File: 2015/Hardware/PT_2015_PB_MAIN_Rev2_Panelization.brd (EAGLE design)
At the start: 142.5 x 234.8 mm, 161 parts, among them Q1 Q_ACS711LC_SKETCH, Q11 Q_IRFS7437PbF, Q12 2N7002, Q14 Q_IRFS7437PbF, Q16 Q_IRFS7437PbF, Q18 Q_FDT86102LZ, Q20 Q_IRFS7437PbF, Q4 Q_ACS711LC, Q5 Q_ACS711LC, Q6 Q_IRFS7437PbF, Q7 Q_IRFS7437PbF, Q9 Q_IRFS7437PbF

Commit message: Cleaned up my idiotic TSTOP
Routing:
- net N$33: track 10.2 -> 0.00 mm
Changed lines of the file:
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@@
 <vertex x="5.08" y="2.54"/>
 </polygon>
-<dimension x1="137.795" y1="166.37" x2="137.795" y2="-67.945" x3="180.34" y3="49.2125" textsize="1.778" layer="21" unit="inch"/>
 <wire x1="1.27" y1="-8.89" x2="104.14" y2="-8.89" width="0.4064" layer="21"/>
 <wire x1="1.27" y1="-8.89" x2="1.27" y2="-52.07" width="0.4064" layer="21"/>
@@
 <wire x1="73.66" y1="-52.07" x2="104.14" y2="-52.07" width="0.4064" layer="21"/>
 <wire x1="104.14" y1="-52.07" x2="104.14" y2="-8.89" width="0.4064" layer="21"/>
+<dimension x1="137.795" y1="166.37" x2="137.541" y2="-68.453" x3="165.69279375" y3="48.928184375" textsize="3.81" layer="29" unit="inch" visible="yes"/>
 <polygon width="0.8128" layer="29">
-<vertex x="45.466" y="119.888"/>
-<vertex x="45.466" y="110.998"/>
-<vertex x="40.894" y="110.998"/>
-<vertex x="40.894" y="103.886"/>
-<vertex x="45.466" y="103.886"/>
-<vertex x="57.658" y="103.886"/>
-<vertex x="57.658" y="105.918"/>
-<vertex x="51.562" y="105.918"/>
-<vertex x="51.562" y="109.728"/>
-<vertex x="51.562" y="111.506"/>
-<vertex x="62.992" y="111.506"/>
-<vertex x="75.184" y="111.506"/>
-<vertex x="75.184" y="105.918"/>
-<vertex x="69.342" y="105.918"/>
-<vertex x="69.342" y="104.14"/>
-<vertex x="82.042" y="104.14"/>
-<vertex x="82.042" y="120.396"/>
-<vertex x="45.466" y="120.396"/>
+<vertex x="71.882" y="1.27"/>
+<vertex x="71.882" y="1.27"/>
+<vertex x="72.136" y="1.27"/>
 </polygon>
 <polygon width="0.8128" layer="29">
-<vertex x="57.658" y="104.902"/>
-<vertex x="69.342" y="104.902"/>
-<vertex x="69.342" y="104.14"/>
-<vertex x="57.658" y="104.14"/>
-<vertex x="57.658" y="103.886"/>
-</polygon>
-<polygon width="0.8128" layer="29">
-<vertex x="63.754" y="104.394"/>
-<vertex x="63.754" y="101.854"/>
-<vertex x="64.516" y="101.854" curve="-90"/>
-<vertex x="71.12" y="95.25" curve="-96.025575"/>
-<vertex x="63.5" y="88.392"/>
-<vertex x="63.5" y="83.058"/>
-<vertex x="64.516" y="83.058" curve="-90"/>
-<vertex x="71.374" y="76.2" curve="-97.62815"/>
-<vertex x="63.246" y="69.088"/>
-<vertex x="63.5" y="69.088"/>
-<vertex x="63.5" y="64.008"/>
-<vertex x="64.516" y="64.008" curve="-90"/>
-<vertex x="71.374" y="57.15" curve="-95.631113"/>
-<vertex x="63.246" y="49.784"/>
-<vertex x="63.246" y="44.958"/>
-<vertex x="64.77" y="44.958" curve="-90"/>
-<vertex x="71.628" y="38.1" curve="-90"/>
-<vertex x="64.516" y="30.988"/>
-<vertex x="63.246" y="30.988"/>
-<vertex x="63.246" y="6.35"/>
-<vertex x="81.026" y="6.35"/>
-<vertex x="81.026" y="23.622"/>
-<vertex x="79.248" y="23.622"/>
-<vertex x="79.248" y="26.67"/>
-<vertex x="81.026" y="26.67"/>
-<vertex x="81.026" y="53.594"/>
-<vertex x="80.01" y="53.594"/>
-<vertex x="80.01" y="104.14"/>
-<vertex x="73.914" y="104.14"/>
-<vertex x="73.914" y="104.394"/>
-</polygon>
-<polygon width="0.8128" layer="29">
-<vertex x="62.992" y="104.648"/>
-<vertex x="62.992" y="102.108"/>
-<vertex x="62.738" y="102.108" curve="90"/>
-<vertex x="56.642" y="96.012"/>
-<vertex x="56.642" y="94.742"/>
-<vertex x="56.642" y="94.488" curve="90"/>
-<vertex x="62.738" y="88.392" curve="-90"/>
-<vertex x="62.992" y="88.138"/>
-<vertex x="62.992" y="83.058"/>
-<vertex x="62.738" y="83.058" curve="90"/>
-<vertex x="56.642" y="76.962"/>
-<vertex x="56.642" y="75.692" curve="90"/>
-<vertex x="63.246" y="69.088"/>
-<vertex x="63.246" y="64.008"/>
-<vertex x="62.992" y="64.008" curve="90"/>
-<vertex x="56.642" y="57.658"/>
-<vertex x="56.642" y="56.642" curve="90"/>
-<vertex x="62.738" y="50.546"/>
-<vertex x="62.738" y="45.212" curve="90"/>
-<vertex x="56.642" y="39.116"/>
-<vertex x="56.642" y="37.592" curve="90"/>
-<vertex x="62.992" y="31.242"/>
-<vertex x="63.246" y="31.242"/>
-<vertex x="63.246" y="-1.778"/>
-<vertex x="60.198" y="-1.778"/>
-<vertex x="51.562" y="-1.778"/>
-<vertex x="49.784" y="0"/>
-<vertex x="48.514" y="1.27"/>
-<vertex x="48.514" y="2.54"/>
-<vertex x="48.514" y="3.302"/>
-<vertex x="47.498" y="3.302"/>
-<vertex x="47.498" y="5.334"/>
+<vertex x="45.974" y="120.65"/>
+<vertex x="45.974" y="110.236"/>
+<vertex x="41.402" y="110.236"/>
+<vertex x="41.402" y="104.394"/>
+<vertex x="45.974" y="104.394"/>
+<vertex x="45.974" y="93.726"/>
+<vertex x="41.402" y="93.726"/>
+<vertex x="41.402" y="87.884"/>
+<vertex x="45.974" y="87.884"/>
+<vertex x="45.974" y="77.216"/>
+<vertex x="41.402" y="77.216"/>
+<vertex x="41.402" y="71.374"/>
+<vertex x="45.974" y="71.374"/>
+<vertex x="45.974" y="60.706"/>
+<vertex x="41.402" y="60.706"/>
+<vertex x="41.402" y="54.864"/>
+<vertex x="45.974" y="54.864"/>
+<vertex x="45.974" y="44.196"/>
+<vertex x="41.402" y="44.196"/>
+<vertex x="41.402" y="38.354"/>
+<vertex x="45.974" y="38.354"/>
+<vertex x="45.974" y="27.686"/>
+<vertex x="41.402" y="27.686"/>
+<vertex x="41.402" y="21.844"/>
+<vertex x="45.974" y="21.844"/>
+<vertex x="45.974" y="11.176"/>
+<vertex x="41.402" y="11.176"/>
 <vertex x="41.402" y="5.334"/>
-<vertex x="41.402" y="11.176"/>
-<vertex x="45.72" y="11.176"/>
-<vertex x="45.974" y="11.176"/>
-<vertex x="45.974" y="21.844"/>
-<vertex x="41.402" y="21.844"/>
-<vertex x="41.402" y="27.686"/>
-<vertex x="45.974" y="27.686"/>
-<vertex x="45.974" y="38.354"/>
-<vertex x="45.72" y="38.354"/>
-<vertex x="41.402" y="38.354"/>
-<vertex x="41.402" y="44.196"/>
-<vertex x="45.974" y="44.196"/>
-<vertex x="45.974" y="54.864"/>
-<vertex x="41.402" y="54.864"/>
-<vertex x="41.402" y="60.706"/>
-<vertex x="46.228" y="60.706"/>
-<vertex x="45.974" y="60.706"/>
-<vertex x="45.974" y="71.374"/>
-<vertex x="41.402" y="71.374"/>
-<vertex x="41.402" y="77.216"/>
-<vertex x="45.974" y="77.216"/>
-<vertex x="45.974" y="87.884"/>
-<vertex x="41.402" y="87.884"/>
-<vertex x="41.402" y="93.726"/>
-<vertex x="45.974" y="93.726"/>
-<vertex x="45.974" y="104.648"/>
-</polygon>
-<polygon width="0.8128" layer="29">
-<vertex x="63.5" y="-1.778"/>
-<vertex x="67.818" y="-1.778"/>
-<vertex x="67.818" y="2.794"/>
-<vertex x="67.818" y="5.08"/>
-<vertex x="71.12" y="5.08"/>
-<vertex x="73.914" y="5.08"/>
-<vertex x="73.914" y="6.35"/>
-<vertex x="81.026" y="6.35"/>
-<vertex x="81.026" y="8.128"/>
-<vertex x="79.248" y="8.128"/>
-<vertex x="63.5" y="8.128"/>
-</polygon>
-<polygon width="0.8128" layer="29">
-<vertex x="67.818" y="1.524"/>
-<vertex x="67.818" y="1.27"/>
-<vertex x="72.136" y="1.27"/>
-<vertex x="72.136" y="0"/>
-<vertex x="81.026" y="0"/>
+<vertex x="45.974" y="5.334"/>
+<vertex x="49.53" y="5.334"/>
+<vertex x="49.53" y="0.508"/>
+<vertex x="53.086" y="0.508"/>
+<vertex x="53.086" y="-1.778"/>
+<vertex x="60.96" y="-1.778"/>
 <vertex x="81.026" y="-1.778"/>
-<vertex x="67.818" y="-1.778"/>
-<vertex x="67.818" y="1.27"/>
+<vertex x="81.026" y="12.954"/>
+<vertex x="79.248" y="12.954"/>
+<vertex x="79.248" y="34.29"/>
+<vertex x="81.026" y="34.29"/>
+<vertex x="81.026" y="36.83"/>
+<vertex x="81.026" y="47.752"/>
+<vertex x="79.502" y="47.752"/>
+<vertex x="79.502" y="55.118"/>
+<vertex x="79.502" y="71.628"/>
+<vertex x="79.756" y="71.628"/>
+<vertex x="79.756" y="119.126"/>
+<vertex x="79.756" y="119.888"/>
+<vertex x="77.47" y="119.888"/>
+<vertex x="57.404" y="119.888"/>
+<vertex x="57.404" y="113.03"/>
+<vertex x="75.438" y="113.03"/>
+<vertex x="75.438" y="104.14"/>
+<vertex x="57.404" y="104.14"/>
+<vertex x="57.404" y="113.03"/>
+<vertex x="57.404" y="98.044"/>
+<vertex x="72.136" y="98.044"/>
+<vertex x="72.136" y="92.71"/>
+<vertex x="57.404" y="92.71"/>
+<vertex x="57.404" y="98.044"/>
+<vertex x="57.404" y="73.406"/>
+<vertex x="72.39" y="73.406"/>
+<vertex x="72.39" y="80.01"/>
+<vertex x="57.404" y="80.01"/>
+<vertex x="57.404" y="54.61"/>
+<vertex x="72.136" y="54.61"/>
+<vertex x="72.136" y="60.198"/>
+<vertex x="57.404" y="60.198"/>
+<vertex x="57.404" y="35.56"/>
+<vertex x="72.898" y="35.56"/>
+<vertex x="72.898" y="42.672"/>
+<vertex x="57.404" y="42.672"/>
+<vertex x="57.404" y="120.396"/>
+<vertex x="45.974" y="120.396"/>
 </polygon>
 </plain>
@@
 <vertex x="68.326" y="-49.276"/>
 <vertex x="19.05" y="-49.276"/>
-<vertex x="19.05" y="-71.374"/>
-<vertex x="69.342" y="-71.374"/>
+<vertex x="19.05" y="-67.818"/>
+<vertex x="69.342" y="-67.818"/>
 <vertex x="69.342" y="-50.292"/>
 </polygon>
@@
 <wire x1="97.79" y1="46.863" x2="97.79" y2="44.2625" width="0.3048" layer="1"/>
 </signal>
-<signal name="N$33">
-<wire x1="62.23" y1="107.95" x2="63.5" y2="107.95" width="0.254" layer="1"/>
-<wire x1="63.5" y1="107.95" x2="63.627" y2="107.95" width="0.254" layer="1"/>
-<wire x1="63.627" y1="107.95" x2="64.77" y2="107.95" width="0.254" layer="1"/>
-<wire x1="66.04" y1="107.95" x2="64.77" y2="107.95" width="0.254" layer="1"/>
-<wire x1="64.77" y1="107.95" x2="64.77" y2="108.458" width="0.254" layer="1"/>
-<wire x1="64.77" y1="108.458" x2="63.627" y2="107.95" width="0.254" layer="1"/>
-<wire x1="63.627" y1="107.95" x2="64.77" y2="107.442" width="0.254" layer="1"/>
-<wire x1="64.77" y1="107.442" x2="64.77" y2="107.95" width="0.254" layer="1"/>
-<wire x1="64.77" y1="108.458" x2="63.5" y2="107.95" width="0.254" layer="1"/>
-<wire x1="63.5" y1="107.95" x2="63.5" y2="108.585" width="0.254" layer="1"/>
-<wire x1="63.5" y1="107.95" x2="63.5" y2="107.442" width="0.254" layer="1"/>
-<wire x1="63.5" y1="107.442" x2="63.881" y2="107.442" width="0.254" layer="1"/>
-</signal>
 <signal name="N$34">

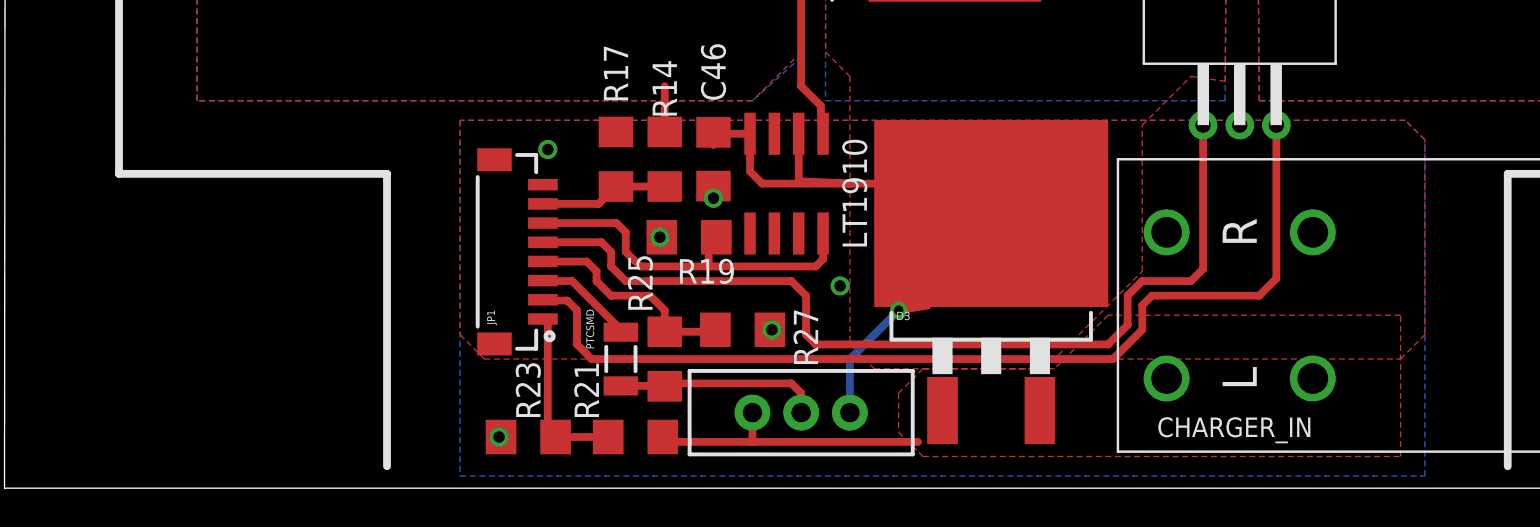
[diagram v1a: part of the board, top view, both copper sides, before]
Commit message: Fixed the connector on SSR portion
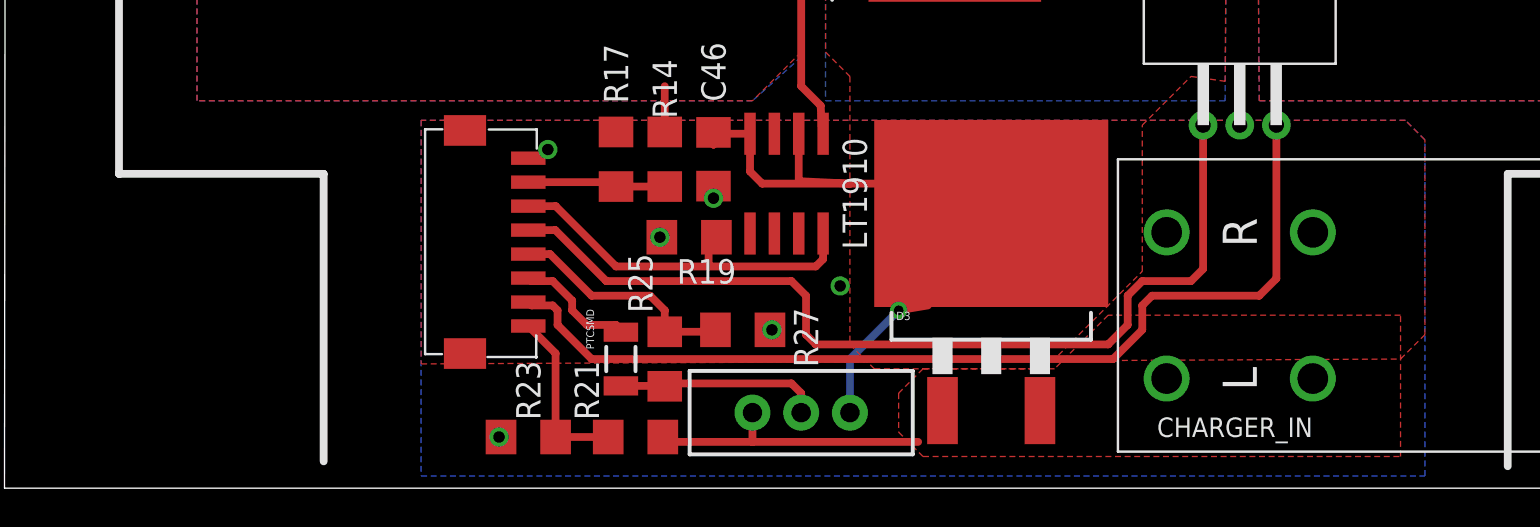
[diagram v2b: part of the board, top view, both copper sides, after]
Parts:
- removed JP1: (no value), SparkFun-Connectors:BM08B-SRSS-TB
- added U$24: 8POS_LOGIC, New:LOGIC_CONNECT
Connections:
- net 5V_SSR: now also U$24.5; no longer JP1.5
- net GATE: now also U$24.6; no longer JP1.6
- net GND: now also U$24.8; no longer JP1.8
- net I_ARRAY: now also U$24.2; no longer JP1.2
- net LOGIC_POWER: now also U$24.3; no longer JP1.3
- net V_CHECK: now also U$24.4; no longer JP1.4
- net V_CHG: now also U$24.1; no longer JP1.1
- net V_OUT: now also U$24.7; no longer JP1.7
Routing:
- net LOGIC_POWER: track 5.37 -> 6.49 mm
- net V_CHECK: track 11.5 -> 12.1 mm
- net 5V_SSR: track 48.3 -> 48.9 mm
- net GATE: track 19.4 -> 20.0 mm

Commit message: Switched out the SSR to meet 3oz Spec
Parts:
- removed U$24: 8POS_LOGIC, New:LOGIC_CONNECT
- added JP1: (no value), SparkFun-Connectors:BM08B-SRSS-TB
- moved V_ARRAY 12.8 mm to (95.2, -27.9)
- moved F1 8.98 mm to (36.3, -60.5)
- moved R21 8.98 mm to (37.1, -64.5)
- moved C46 8.98 mm to (41.1, -50.0)
- moved D3 8.98 mm to (55.6, -54.9)
- moved IRLS3034-7P 8.98 mm to (52.8, -19.1)
- moved IRLS3034-7P.2 8.98 mm to (52.8, -36.8)
- moved R19 8.98 mm to (39.9, -54.1)
- moved R27 8.98 mm to (42.7, -58.9)
- moved S1 8.98 mm to (45.7, -63.2)
- moved U$22 8.98 mm to (68.6, -48.3)
- moved U$23 8.98 mm to (45.0, -51.3)
- moved CHARGER_IN 8.98 mm to (68.6, -57.7)
- moved R14 8.98 mm to (38.6, -50.0)
- moved R17 8.98 mm to (36.1, -50.0)
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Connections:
- removed net GND: 12V-AUX.L1, 12V-AUX.L2, 12V-CRIT.L, 5V-EXT.L, 5V-INT.L, ARM_P.L, AUX_P.L1, AUX_P.L2, BATT-NEG.P$1, C1.-, C10.1, C11.2, C12.2, C13.1, C14.1, C15.1, C16.1, C17.2, C18.2, C19.2, C2.-, C20.2, C21.-, C22.-, C23.1, C24.1, C25.1, C26.1, C27.2, C28.1, C29.1, C3.-, C30.1, C31.2, C32.1, C33.1, C34.1, C35.2, C36.1, C37.2, C38.2, C39.1, C4.-, C40.2, C41.1, C42.2, C43.2, C44.2, C45.-, C46.2, C5.1, C6.1, C7.2, C8.2, C9.2, CHARGER_IN.R1, CHARGER_IN.R2, D1.A, D2.A, DOOKU-12V-CRIT.1, DOOKU-12V-CRIT.7, LED1.C, LED10.C, LED11.C, LED12.C, LED13.C, LED14.C, LED2.C, LED3.C, LED4.C, LED5.C, LED6.C, LED7.C, LED8.C, LED9.C, MOTOR_1.L1, MOTOR_1.L2, MOTOR_2.L1, MOTOR_2.L2, MOTOR_3.L1, MOTOR_3.L2, MOTOR_4.L1, MOTOR_4.L2, MOTOR_5.L1, MOTOR_5.L2, MOTOR_6.L1, MOTOR_6.L2, OKI-78SR-5/1.5-W36H.2, PALPATINE-12V.3, PALPATINE-12V.4, Q1.5, Q12.2, Q4.5, Q5.5, R17.2, R19.2, R23.2, R27.1, R4.1, R7.1, R8.1, SG1.+, SIDEOUS-12V.3, SIDEOUS-12V.4, U$1.15, U$1.17, U$10.1, U$11.1, U$12.1, U$13.1, U$14.5, U$15.5, U$16.5, U$17.5, U$18.5, U$19.5, U$2.2, U$20.5, U$21.5, U$22.2, U$23.1, U$24.8, U$3.GND, U$4.7, U$4.8, U$5.2, U$6.1, U$7.1, U$8.1, U$9.1, VADER-5V-EXT.1, VADER-5V-EXT.7
- new net 0: 12V-AUX.L1, 12V-AUX.L2, 12V-CRIT.L, 5V-EXT.L, 5V-INT.L, ARM_P.L, AUX_P.L1, AUX_P.L2, BATT-NEG.P$1, C1.-, C10.1, C11.2, C12.2, C13.1, C14.1, C15.1, C16.1, C17.2, C18.2, C19.2, C2.-, C20.2, C21.-, C22.-, C23.1, C24.1, C25.1, C26.1, C27.2, C28.1, C29.1, C3.-, C30.1, C31.2, C32.1, C33.1, C34.1, C35.2, C36.1, C37.2, C38.2, C39.1, C4.-, C40.2, C41.1, C42.2, C43.2, C44.2, C45.-, C5.1, C6.1, C7.2, C8.2, C9.2, D1.A, D2.A, DOOKU-12V-CRIT.1, DOOKU-12V-CRIT.7, LED1.C, LED10.C, LED11.C, LED12.C, LED13.C, LED14.C, LED2.C, LED3.C, LED4.C, LED5.C, LED6.C, LED7.C, LED8.C, LED9.C, MOTOR_1.L1, MOTOR_1.L2, MOTOR_2.L1, MOTOR_2.L2, MOTOR_3.L1, MOTOR_3.L2, MOTOR_4.L1, MOTOR_4.L2, MOTOR_5.L1, MOTOR_5.L2, MOTOR_6.L1, MOTOR_6.L2, OKI-78SR-5/1.5-W36H.2, PALPATINE-12V.3, PALPATINE-12V.4, Q1.5, Q12.2, Q4.5, Q5.5, R4.1, R7.1, R8.1, SG1.+, SIDEOUS-12V.3, SIDEOUS-12V.4, U$1.15, U$1.17, U$10.1, U$11.1, U$12.1, U$13.1, U$14.5, U$15.5, U$16.5, U$17.5, U$18.5, U$19.5, U$2.2, U$20.5, U$21.5, U$3.GND, U$4.7, U$4.8, U$5.2, U$6.1, U$7.1, U$8.1, U$9.1, VADER-5V-EXT.1, VADER-5V-EXT.7
- new net GND_SSR: C46.2, CHARGER_IN.R1, CHARGER_IN.R2, JP1.8, R17.2, R19.2, R23.2, R27.1, U$22.2, U$23.1
- net 5V_SSR: now also JP1.5; no longer U$24.5
- net GATE: now also JP1.6; no longer U$24.6
- net I_ARRAY: now also JP1.2; no longer U$24.2
- net LOGIC_POWER: now also JP1.3; no longer U$24.3
- net V_CHECK: now also JP1.4; no longer U$24.4
- net V_CHG: now also JP1.1; no longer U$24.1
- net V_OUT: now also JP1.7; no longer U$24.7
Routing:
- net 5V_SSR: track 48.9 -> 46.8 mm
- net LOGIC_POWER: track 6.49 -> 5.37 mm
- net I_ARRAY: track 51.1 -> 50.3 mm
- net N$356: track 30.4 -> 29.7 mm
- net V_CHECK: track 12.1 -> 11.5 mm
- net GATE: track 20.0 -> 19.4 mm
- net GND: track 0.23 -> 0.00 mm, vias 39 -> 0
- net 0: track 0.00 -> 0.13 mm, vias 0 -> 33
- net GND_SSR: track 0.00 -> 0.10 mm, vias 0 -> 6
- added copper zone on layer 1, net 0
- added copper zone on layer 16, net 0
- added copper zone on layer 1, net GND_SSR
- added copper zone on layer 16, net GND_SSR
- removed copper zone on layer 1, net GND
- removed copper zone on layer 16, net GND
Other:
- board size 142.5 x 234.8 mm -> 145 x 234.8 mm
